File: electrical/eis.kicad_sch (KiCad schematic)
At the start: 12 parts

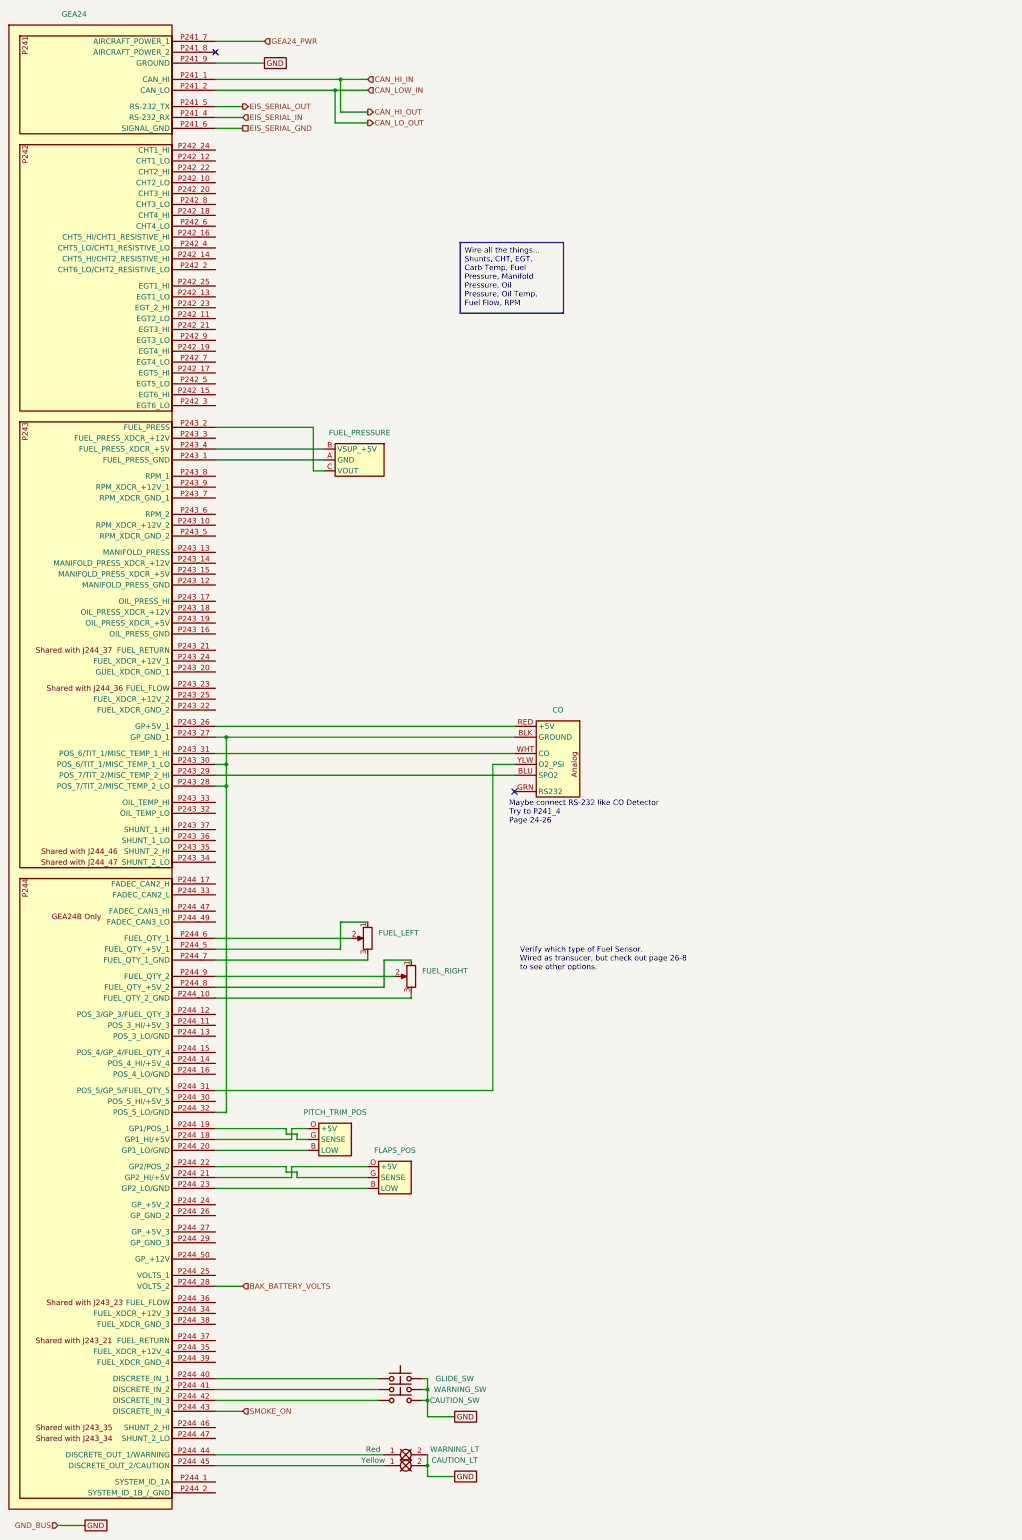
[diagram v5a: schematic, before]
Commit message: Changed to have ELT with GPS. Also, changed Flaps to have position sensor. Added in wiring for all the sensors.
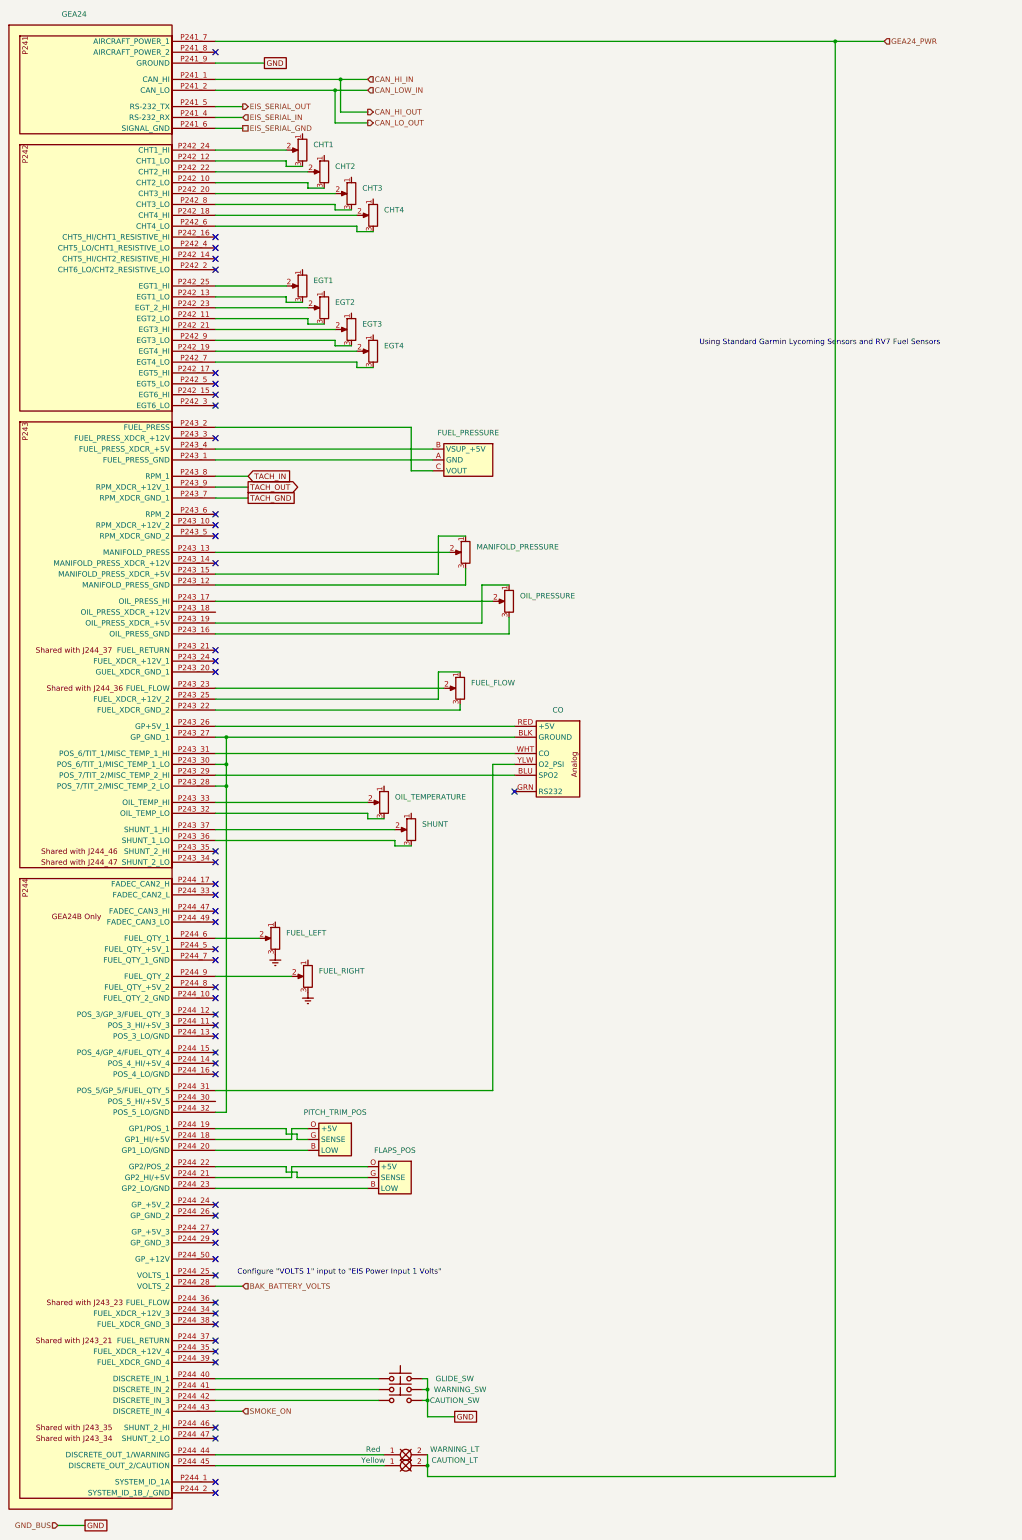
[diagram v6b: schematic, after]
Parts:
- added CHT1, CHT2, CHT3, CHT4, EGT1, EGT2, EGT3, EGT4, FUEL_FLOW, MANIFOLD_PRESSURE, OIL_PRESSURE, OIL_TEMPERATURE, SHUNT: FUEL_QTY_SENSOR, symbol Device:R_Potentiometer
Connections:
- net GEA24_PWR: now also CAUTION_LT.2, WARNING_LT.2
- net GND: no longer CAUTION_LT.2, WARNING_LT.2
- net at FUEL_RIGHT.1: no longer GEA24.P244_8 (FUEL_QTY_+5V_2)
- net at GEA24.P244_10 (FUEL_QTY_2_GND): no longer FUEL_RIGHT.3
- net at FUEL_LEFT.1: no longer GEA24.P244_5 (FUEL_QTY_+5V_1)
- net at GEA24.P244_7 (FUEL_QTY_1_GND): no longer FUEL_LEFT.3
- net at GEA24.P242_10 (CHT2_LO): now also CHT2.3
- net at GEA24.P242_11 (EGT2_LO): now also EGT2.3
- net at GEA24.P242_12 (CHT1_LO): now also CHT1.3
- net at GEA24.P242_13 (EGT1_LO): now also EGT1.3
- net at GEA24.P242_18 (CHT4_HI): now also CHT4.2
- net at GEA24.P242_19 (EGT4_HI): now also EGT4.2
- net at GEA24.P242_20 (CHT3_HI): now also CHT3.2
- net at GEA24.P242_21 (EGT3_HI): now also EGT3.2
- net at GEA24.P242_22 (CHT2_HI): now also CHT2.2
- net at GEA24.P242_23 (EGT_2_HI): now also EGT2.2
- net at GEA24.P242_24 (CHT1_HI): now also CHT1.2
- net at GEA24.P242_25 (EGT1_HI): now also EGT1.2
- net at GEA24.P242_6 (CHT4_LO): now also CHT4.3
- net at GEA24.P242_7 (EGT4_LO): now also EGT4.3
- net at GEA24.P242_8 (CHT3_LO): now also CHT3.3
- net at GEA24.P242_9 (EGT3_LO): now also EGT3.3
- net at GEA24.P243_12 (MANIFOLD_PRESS_GND): now also MANIFOLD_PRESSURE.3
- net at GEA24.P243_13 (MANIFOLD_PRESS): now also MANIFOLD_PRESSURE.2
- net at GEA24.P243_15 (MANIFOLD_PRESS_XDCR_+5V): now also MANIFOLD_PRESSURE.1
- net at GEA24.P243_16 (OIL_PRESS_GND): now also OIL_PRESSURE.3
- net at GEA24.P243_17 (OIL_PRESS_HI): now also OIL_PRESSURE.2
- net at GEA24.P243_19 (OIL_PRESS_XDCR_+5V): now also OIL_PRESSURE.1
- net at GEA24.P243_22 (FUEL_XDCR_GND_2): now also FUEL_FLOW.3
- net at GEA24.P243_23 (FUEL_FLOW): now also FUEL_FLOW.2
- net at GEA24.P243_25 (FUEL_XDCR_+12V_2): now also FUEL_FLOW.1
- net at GEA24.P243_32 (OIL_TEMP_LO): now also OIL_TEMPERATURE.3
- net at GEA24.P243_33 (OIL_TEMP_HI): now also OIL_TEMPERATURE.2
- net at GEA24.P243_36 (SHUNT_1_LO): now also SHUNT.3
- net at GEA24.P243_37 (SHUNT_1_HI): now also SHUNT.2
- net TACH_GND: now reaches GEA24.P243_7 (RPM_XDCR_GND_1)
- net TACH_IN: now reaches GEA24.P243_8 (RPM_1)
- net TACH_OUT: now reaches GEA24.P243_9 (RPM_XDCR_+12V_1)
- new net Earth: FUEL_LEFT.3, FUEL_RIGHT.3
- no-connect marks 2 -> 50
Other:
- note added: "Configure "VOLTS 1" input to "EIS Power Input 1 Volts""
- note added: "Using Standard Garmin Lycoming Sensors and RV7 Fuel Sensors"
- note removed: "Maybe connect RS-232 like CO Detector Try to P241_4 Page 24-26"
- note removed: "Verify which type of Fuel Sensor. Wired as transucer, but check out page 26-8 to see other options."
- moved on the sheet: FUEL_LEFT, FUEL_PRESSURE, FUEL_RIGHT

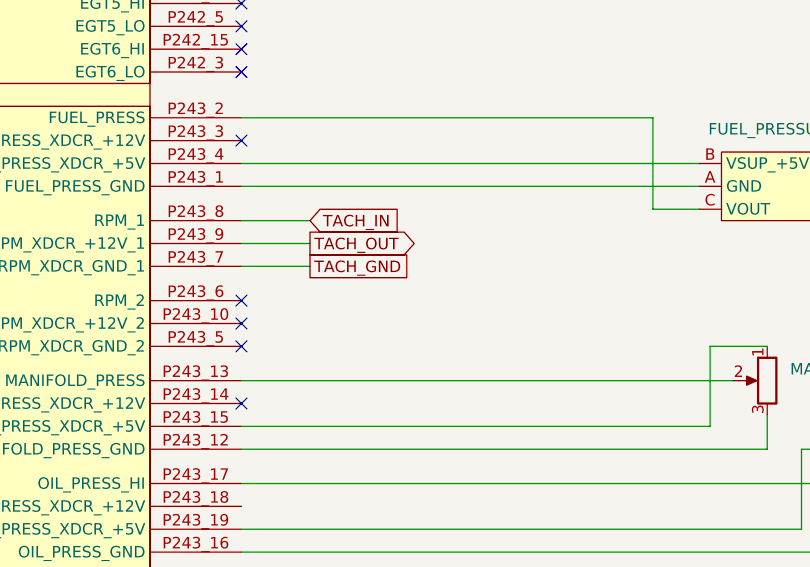
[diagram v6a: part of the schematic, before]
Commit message: Changed GTR CB to 7.5A. Added engine instrumentation. Added signal for fuel on.
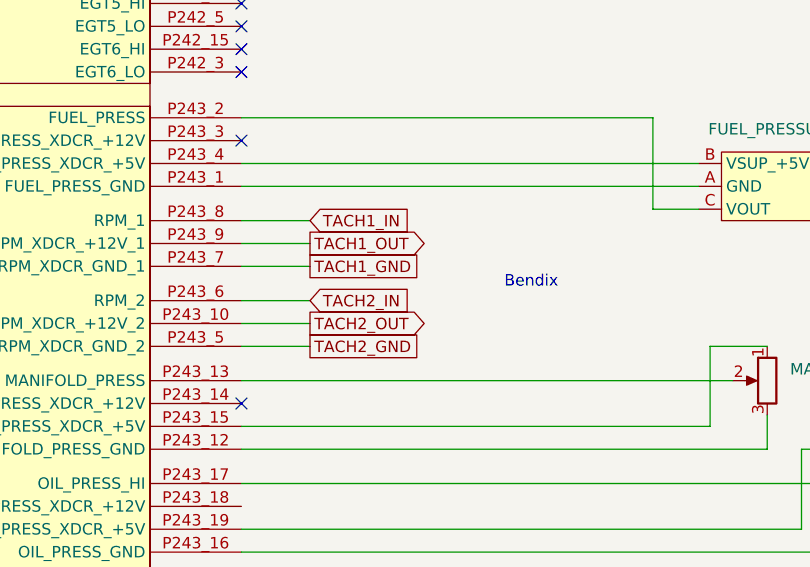
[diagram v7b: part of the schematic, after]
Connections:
- net TACH2_OUT: now reaches GEA24.P243_10 (RPM_XDCR_+12V_2)
- net TACH2_GND: now reaches GEA24.P243_5 (RPM_XDCR_GND_2)
- net TACH2_IN: now reaches GEA24.P243_6 (RPM_2)
- net TACH_GND renamed TACH1_GND
- net TACH_IN renamed TACH1_IN
- net TACH_OUT renamed TACH1_OUT
- no-connect marks 50 -> 47
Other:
- note added: "Bendix"
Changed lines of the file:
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@@
   (title_block
     (title "EIS")
-    (date "2024-02-14")
-    (rev "0.9.3")
+    (date "2024-05-02")
+    (rev "0.9.4")
     (company "N877RV")
   )
@@
   (no_connect (at 67.31 224.79))
   (no_connect (at 67.31 213.36))
-  (no_connect (at 67.31 132.08))
   (no_connect (at 67.31 293.37))
   (no_connect (at 67.31 74.93))
@@
   (no_connect (at 67.31 67.31))
   (no_connect (at 67.31 69.85))
-  (no_connect (at 67.31 134.62))
   (no_connect (at 137.16 196.85))
   (no_connect (at 67.31 330.2))
@@
   (no_connect (at 67.31 306.07))
   (no_connect (at 67.31 220.98))
-  (no_connect (at 67.31 137.16))
   (no_connect (at 67.31 245.11))
   (no_connect (at 67.31 248.92))
@@
     (stroke (width 0) (type default))
   )
+  (wire (pts (xy 67.31 137.16) (xy 74.93 137.16))
+    (stroke (width 0) (type default))
+  )
   (wire (pts (xy 88.9 54.61) (xy 88.9 55.88))
     (stroke (width 0) (type default))
@@
     (stroke (width 0) (type default))
   )
+  (wire (pts (xy 67.31 134.62) (xy 74.93 134.62))
+    (stroke (width 0) (type default))
+  )
   (wire (pts (xy 86.36 285.75) (xy 86.36 287.02))
     (stroke (width 0) (type default))
@@
     (stroke (width 0) (type default))
   )
+  (wire (pts (xy 67.31 132.08) (xy 74.93 132.08))
+    (stroke (width 0) (type default))
+  )
   (wire (pts (xy 88.9 55.88) (xy 92.71 55.88))
     (stroke (width 0) (type default))
@@
   (wire (pts (xy 212.09 21.59) (xy 223.52 21.59))
     (stroke (width 0) (type default))
+  )
+  (text "Bendix" (at 96.52 130.81 0)
+    (effects (font (size 1.27 1.27)) (justify left bottom))
   )
   (text "Using Standard Garmin Lycoming Sensors and RV7 Fuel Sensors"
@@
     )
   )
-  (global_label "TACH_OUT" (shape output) (at 74.93 125.73 0) (fields_autoplaced)
-    (effects (font (size 1.27 1.27)) (justify left))
-    (property "Intersheetrefs" "${INTERSHEET_REFS}" (at 87.1681 125.73 0)
+  (global_label "TACH2_GND" (shape passive) (at 74.93 137.16 0) (fields_autoplaced)
+    (effects (font (size 1.27 1.27)) (justify left))
+    (property "Intersheetrefs" "${INTERSHEET_REFS}" (at 87.5082 137.16 0)
+      (effects (font (size 1.27 1.27)) (justify left) hide)
+    )
+  )
+  (global_label "TACH1_OUT" (shape output) (at 74.93 125.73 0) (fields_autoplaced)
+    (effects (font (size 1.27 1.27)) (justify left))
+    (property "Intersheetrefs" "${INTERSHEET_REFS}" (at 88.3776 125.73 0)
       (effects (font (size 1.27 1.27)) (justify left) hide)
     )
@@
     )
   )
-  (global_label "TACH_GND" (shape passive) (at 74.93 128.27 0) (fields_autoplaced)
-    (effects (font (size 1.27 1.27)) (justify left))
-    (property "Intersheetrefs" "${INTERSHEET_REFS}" (at 86.2987 128.27 0)
-      (effects (font (size 1.27 1.27)) (justify left) hide)
-    )
-  )
-  (global_label "TACH_IN" (shape input) (at 74.93 123.19 0) (fields_autoplaced)
-    (effects (font (size 1.27 1.27)) (justify left))
-    (property "Intersheetrefs" "${INTERSHEET_REFS}" (at 85.4748 123.19 0)
-      (effects (font (size 1.27 1.27)) (justify left) hide)
-    )
+  (global_label "TACH1_GND" (shape passive) (at 74.93 128.27 0) (fields_autoplaced)
+    (effects (font (size 1.27 1.27)) (justify left))
+    (property "Intersheetrefs" "${INTERSHEET_REFS}" (at 87.5082 128.27 0)
+      (effects (font (size 1.27 1.27)) (justify left) hide)
+    )
+  )
+  (global_label "TACH1_IN" (shape input) (at 74.93 123.19 0) (fields_autoplaced)
+    (effects (font (size 1.27 1.27)) (justify left))
+    (property "Intersheetrefs" "${INTERSHEET_REFS}" (at 86.6843 123.19 0)
+      (effects (font (size 1.27 1.27)) (justify left) hide)
+    )
+  )
+  (global_label "TACH2_IN" (shape input) (at 74.93 132.08 0) (fields_autoplaced)
+    (effects (font (size 1.27 1.27)) (justify left))
+    (property "Intersheetrefs" "${INTERSHEET_REFS}" (at 86.6843 132.08 0)
+      (effects (font (size 1.27 1.27)) (justify left) hide)
+    )
+  )
+  (global_label "TACH2_OUT" (shape output) (at 74.93 134.62 0) (fields_autoplaced)
+    (effects (font (size 1.27 1.27)) (justify left))
+    (property "Intersheetrefs" "${INTERSHEET_REFS}" (at 88.3776 134.62 0)
+      (effects (font (size 1.27 1.27)) (justify left) hide)
+    )

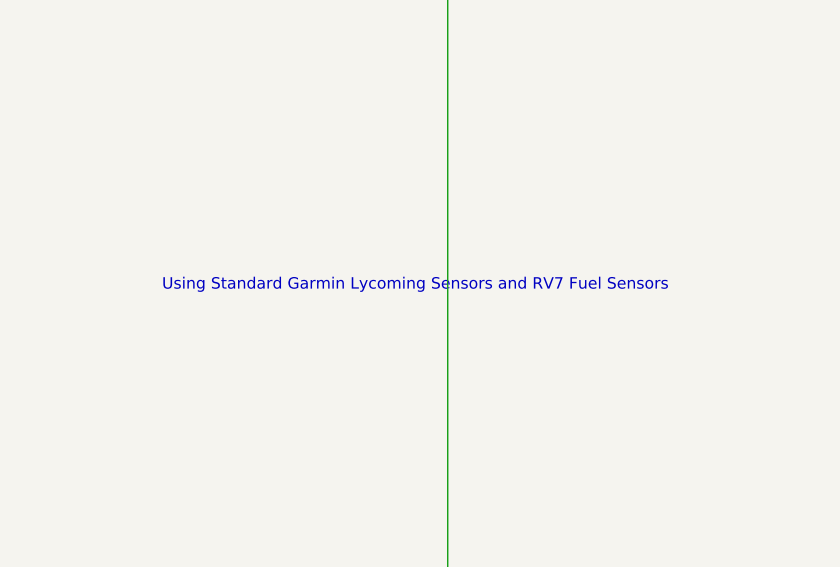
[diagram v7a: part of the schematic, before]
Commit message: Updated canbus diagrams with order for where magnometer and servos will be located. Added yaw servo.
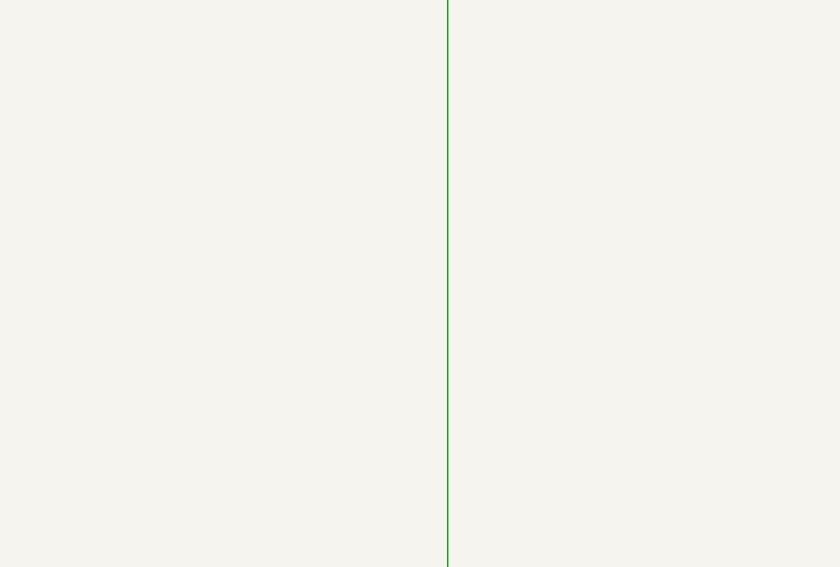
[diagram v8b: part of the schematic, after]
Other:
- note removed: "Using Standard Garmin Lycoming Sensors and RV7 Fuel Sensors"
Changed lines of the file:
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@@
   (title_block
     (title "EIS")
-    (date "2024-05-02")
-    (rev "0.9.4")
+    (date "2024-05-07")
+    (rev "1.0")
     (company "N877RV")
   )
@@
     (effects (font (size 1.27 1.27)) (justify left bottom))
   )
-  (text "Using Standard Garmin Lycoming Sensors and RV7 Fuel Sensors"
-    (at 180.34 92.71 0)
-    (effects (font (size 1.27 1.27)) (justify left bottom))
-  )
